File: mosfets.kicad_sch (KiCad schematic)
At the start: 25 parts, among them IC2 IRFR9014PBF, J4 Screw_Terminal_01x02, J5 Screw_Terminal_01x02, J6 Screw_Terminal_01x02, J7 Screw_Terminal_01x02, J8 Screw_Terminal_01x02, J9 Screw_Terminal_01x02, Q1 DMN3404L, Q2 DMN3404L, Q3 DMN3404L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

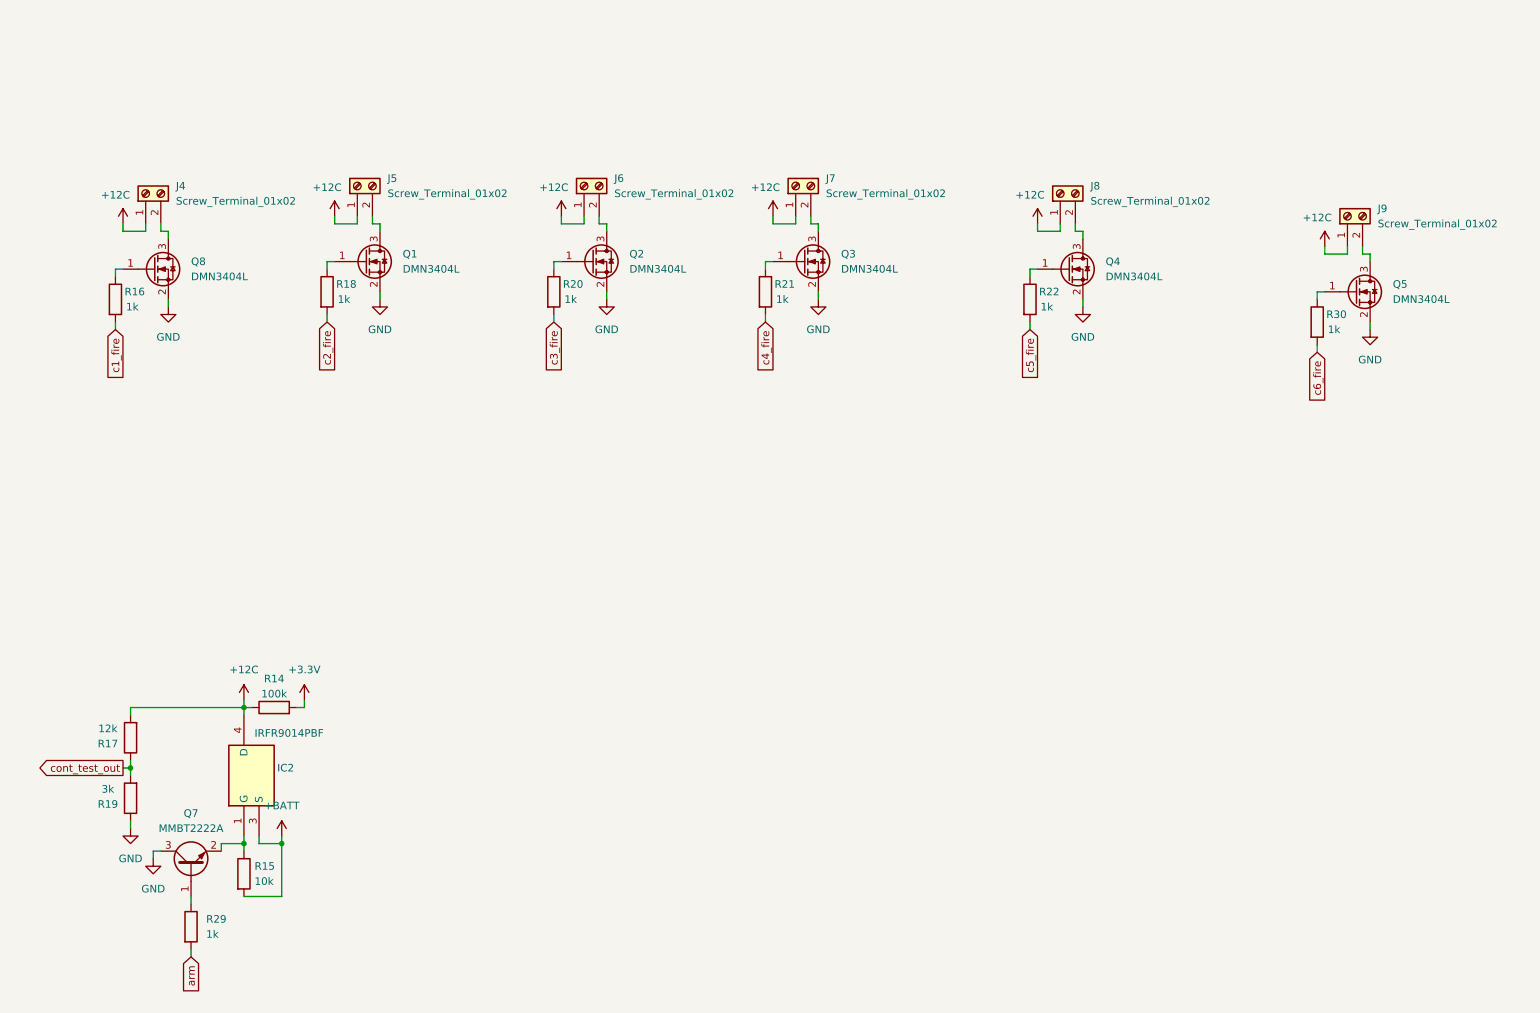
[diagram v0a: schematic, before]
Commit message: placed mosfet stuff, probably all that's left is add pull resistors on the nfets and finish routing the fets
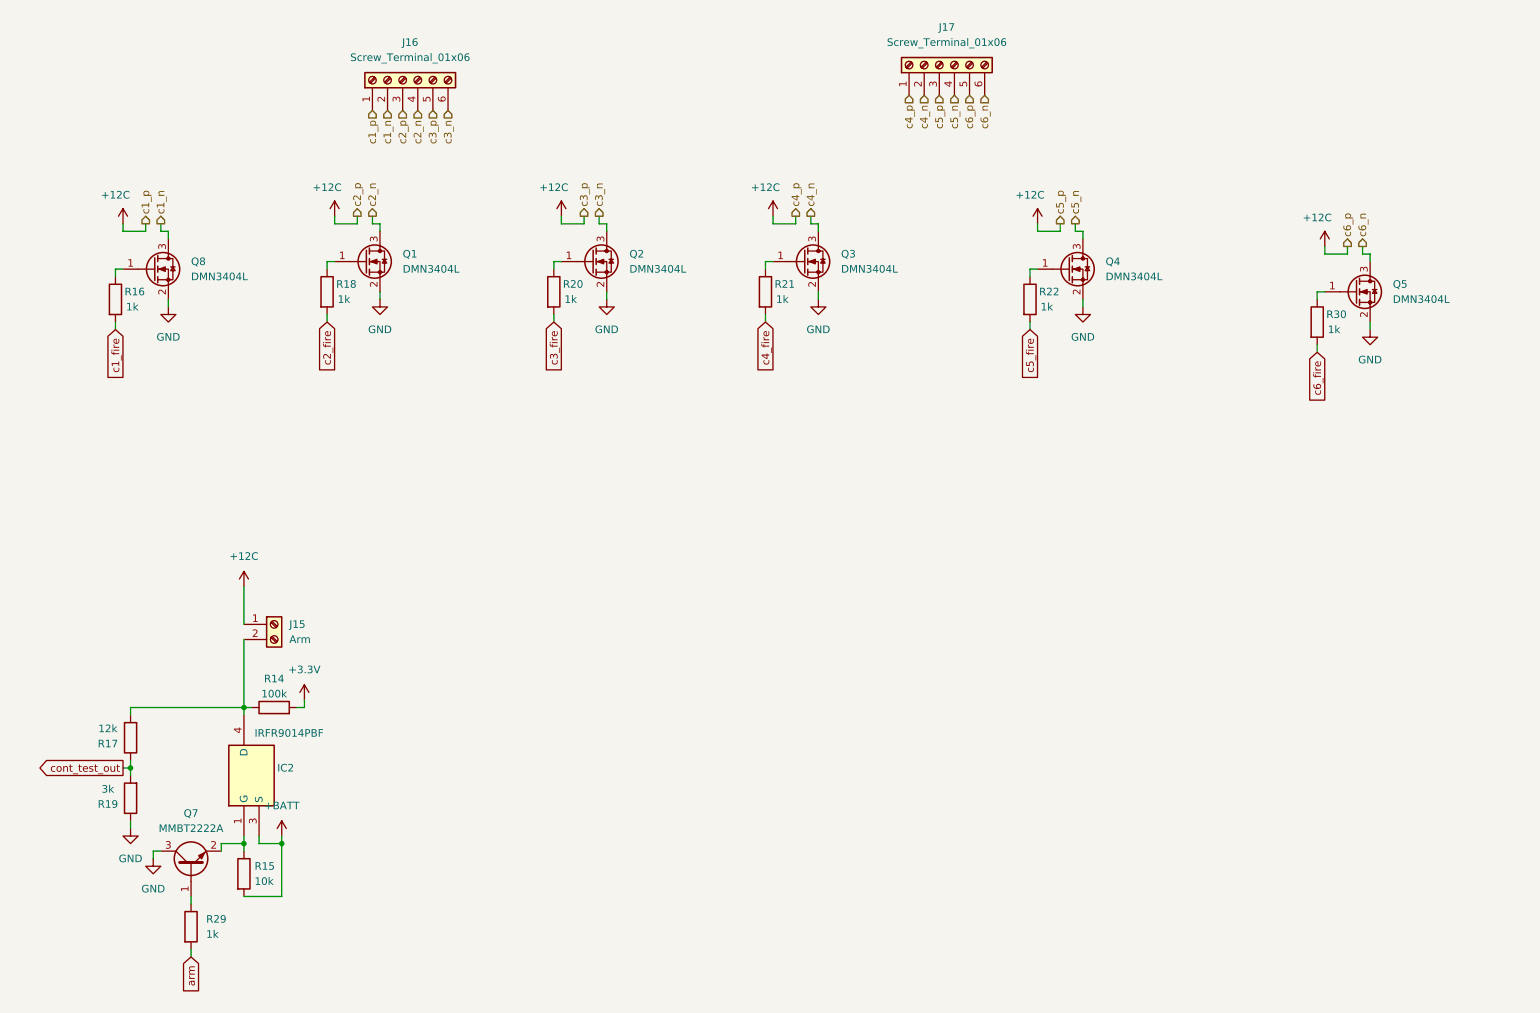
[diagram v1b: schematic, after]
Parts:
- removed J4, J5, J6, J7, J8, J9: Screw_Terminal_01x02, TerminalBlock:TerminalBlock_Xinya_XY308-2.54-2P_1x02_P2.54mm_Horizontal, symbol Connector:Screw_Terminal_01x02
- added J15: Arm, TerminalBlock:TerminalBlock_Xinya_XY308-2.54-2P_1x02_P2.54mm_Horizontal, symbol Connector:Screw_Terminal_01x02
- added J16, J17: Screw_Terminal_01x06, TerminalBlock:TerminalBlock_Xinya_XY308-2.54-6P_1x06_P2.54mm_Horizontal, symbol Connector:Screw_Terminal_01x06
- R14, R15, R16, R17, R18, R19, R20, R21, R22, R30: footprint Resistor_SMD:R_0603_1608Metric -> Resistor_SMD:R_0402_1005Metric
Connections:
- net +12C: now also J15.1 (Pin_1), J16.1 (Pin_1), J16.3 (Pin_3), J16.5 (Pin_5), J17.1 (Pin_1), J17.3 (Pin_3), J17.5 (Pin_5); no longer IC2.4 (D), R14.1, R17.2
- net c4_n: now reaches Q3.3 (D)
- net c4_n: now also J17.2 (Pin_2)
- net c1_n: now reaches Q8.3 (D)
- net c1_n: now also J16.2 (Pin_2)
- net c5_n: now reaches Q4.3 (D)
- net c5_n: now also J17.4 (Pin_4)
- net c2_n: now reaches Q1.3 (D)
- net c2_n: now also J16.4 (Pin_4)
- net c6_n: now reaches Q5.3 (D)
- net c6_n: now also J17.6 (Pin_6)
- net c3_n: now reaches Q2.3 (D)
- net c3_n: now also J16.6 (Pin_6)
- new net: IC2.4 (D), J15.2 (Pin_2), R14.1, R17.2

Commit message: idk what I did but it wasn't saved
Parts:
- removed J16, J17: Screw_Terminal_01x06, TerminalBlock:TerminalBlock_Xinya_XY308-2.54-6P_1x06_P2.54mm_Horizontal, symbol Connector:Screw_Terminal_01x06
- added J4: Screw_Terminal_01x12, TerminalBlock:TerminalBlock_Xinya_XY308-2.54-12P_1x12_P2.54mm_Horizontal, symbol Connector:Screw_Terminal_01x12
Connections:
- net +12C: now also J4.10 (Pin_10), J4.12 (Pin_12), J4.2 (Pin_2), J4.4 (Pin_4), J4.6 (Pin_6), J4.8 (Pin_8)
- net c1_n: now also J4.11 (Pin_11)
- net c2_n: now also J4.9 (Pin_9)
- net c3_n: now also J4.7 (Pin_7)
- net c4_n: now also J4.5 (Pin_5)
- net c5_n: now also J4.3 (Pin_3)
- net c6_n: now also J4.1 (Pin_1)
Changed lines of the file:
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@@
 	(hierarchical_label "c1_n"
 		(shape input)
-		(at 83.82 38.1 270)
+		(at 137.16 34.29 270)
 		(effects
 			(font
@@
 	(hierarchical_label "c3_p"
 		(shape input)
-		(at 91.44 38.1 270)
+		(at 129.54 34.29 270)
 		(effects
 			(font
@@
 	(hierarchical_label "c5_p"
 		(shape input)
-		(at 176.53 35.56 270)
+		(at 119.38 34.29 270)
 		(effects
 			(font
@@
 	(hierarchical_label "c2_p"
 		(shape input)
-		(at 86.36 38.1 270)
+		(at 134.62 34.29 270)
 		(effects
 			(font
@@
 	(hierarchical_label "c3_n"
 		(shape input)
-		(at 93.98 38.1 270)
+		(at 127 34.29 270)
 		(effects
 			(font
@@
 	(hierarchical_label "c6_n"
 		(shape input)
-		(at 184.15 35.56 270)
+		(at 111.76 34.29 270)
 		(effects
 			(font
@@
 	(hierarchical_label "c4_p"
 		(shape input)
-		(at 171.45 35.56 270)
+		(at 124.46 34.29 270)
 		(effects
 			(font
@@
 	(hierarchical_label "c5_n"
 		(shape input)
-		(at 179.07 35.56 270)
+		(at 116.84 34.29 270)
 		(effects
 			(font
@@
 	(hierarchical_label "c4_n"
 		(shape input)
-		(at 173.99 35.56 270)
+		(at 121.92 34.29 270)
 		(effects
 			(font
@@
 	(hierarchical_label "c1_p"
 		(shape input)
-		(at 81.28 38.1 270)
+		(at 139.7 34.29 270)
 		(effects
 			(font
@@
 	(hierarchical_label "c6_p"
 		(shape input)
-		(at 181.61 35.56 270)
+		(at 114.3 34.29 270)
 		(effects
 			(font
@@
 	(hierarchical_label "c2_n"
 		(shape input)
-		(at 88.9 38.1 270)
+		(at 132.08 34.29 270)
 		(effects
 			(font
@@
 	)
 	(symbol
+		(lib_id "Connector:Screw_Terminal_01x12")
+		(at 124.46 29.21 90)
+		(unit 1)
+		(exclude_from_sim no)
+		(in_bom yes)
+		(on_board yes)
+		(dnp no)
+		(fields_autoplaced yes)
+		(property "Reference" "J4"
+			(at 125.73 22.86 90)
+			(effects
+				(font
+					(size 1.27 1.27)
+				)
+			)
+		)
+		(property "Value" "Screw_Terminal_01x12"
+			(at 125.73 25.4 90)
+			(effects
+				(font
+					(size 1.27 1.27)
+				)
+			)
+		)
+		(property "Footprint" "TerminalBlock:TerminalBlock_Xinya_XY308-2.54-12P_1x12_P2.54mm_Horizontal"
+			(at 124.46 29.21 0)
+			(effects
+				(font
+					(size 1.27 1.27)
+				)
+				(hide yes)
+			)
+		)
+		(property "Datasheet" "~"
+			(at 124.46 29.21 0)
+			(effects
+				(font
+					(size 1.27 1.27)
+				)
+				(hide yes)
+			)
+		)
+		(property "Description" "Generic screw terminal, single row, 01x12, script generated (kicad-library-utils/schlib/autogen/connector/)"
+			(at 124.46 29.21 0)
+			(effects
+				(font
+					(size 1.27 1.27)
+				)
+				(hide yes)
+			)
+		)
+		(pin "6"
+		)
+		(pin "10"
+		)
+		(pin "1"
+		)
+		(pin "7"
+		)
+		(pin "5"
+		)
+		(pin "4"
+		)
+		(pin "3"
+		)
+		(pin "12"
+		)
+		(pin "11"
+		)
+		(pin "2"
+		)
+		(pin "9"
+		)
+		(pin "8"
+		)
+		(instances
+			(project ""
+				(path "/d0cafa98-cc2a-4ab3-8dbc-f937bedf434b/95cda17b-9612-4f29-a3fa-5878468b6ce9"
+					(reference "J4")
+					(unit 1)
+				)
+			)
+		)
+	)
+	(symbol
 		(lib_id "power:+12C")
 		(at 74.93 55.88 0)
@@
 	)
 	(symbol
-		(lib_id "Connector:Screw_Terminal_01x06")
-		(at 86.36 33.02 90)
-		(unit 1)
-		(exclude_from_sim no)
-		(in_bom yes)
-		(on_board yes)
-		(dnp no)
-		(fields_autoplaced yes)
-		(property "Reference" "J16"
-			(at 87.63 26.67 90)
-			(effects
-				(font
-					(size 1.27 1.27)
-				)
-			)
-		)
-		(property "Value" "Screw_Terminal_01x06"
-			(at 87.63 29.21 90)
-			(effects
-				(font
-					(size 1.27 1.27)
-				)
-			)
-		)
-		(property "Footprint" "TerminalBlock:TerminalBlock_Xinya_XY308-2.54-6P_1x06_P2.54mm_Horizontal"
-			(at 86.36 33.02 0)
-			(effects
-				(font
-					(size 1.27 1.27)
-				)
-				(hide yes)
-			)
-		)
-		(property "Datasheet" "~"
-			(at 86.36 33.02 0)
-			(effects
-				(font
-					(size 1.27 1.27)
-				)
-				(hide yes)
-			)
-		)
-		(property "Description" "Generic screw terminal, single row, 01x06, script generated (kicad-library-utils/schlib/autogen/connector/)"
-			(at 86.36 33.02 0)
-			(effects
-				(font
-					(size 1.27 1.27)
-				)
-				(hide yes)
-			)
-		)
-		(pin "4"
-		)
-		(pin "3"
-		)
-		(pin "2"
-		)
-		(pin "5"
-		)
-		(pin "1"
-		)
-		(pin "6"
-		)
-		(instances
-			(project ""
-				(path "/d0cafa98-cc2a-4ab3-8dbc-f937bedf434b/95cda17b-9612-4f29-a3fa-5878468b6ce9"
-					(reference "J16")
-					(unit 1)
-				)
-			)
-		)
-	)
-	(symbol
 		(lib_id "Device:R")
 		(at 38.1 69.85 0)
@@
 					(unit 1)
 				)
-			)
-		)
-	)
-	(symbol
-		(lib_id "Connector:Screw_Terminal_01x06")
-		(at 176.53 30.48 90)
-		(unit 1)
-		(exclude_from_sim no)
-		(in_bom yes)
-		(on_board yes)
-		(dnp no)
-		(fields_autoplaced yes)
-		(property "Reference" "J17"
-			(at 177.8 24.13 90)
-			(effects
-				(font
-					(size 1.27 1.27)
-				)
-			)
-		)
-		(property "Value" "Screw_Terminal_01x06"
-			(at 177.8 26.67 90)
-			(effects
-				(font
-					(size 1.27 1.27)
-				)
-			)
-		)
-		(property "Footprint" "TerminalBlock:TerminalBlock_Xinya_XY308-2.54-6P_1x06_P2.54mm_Horizontal"
-			(at 176.53 30.48 0)
-			(effects
-				(font
-					(size 1.27 1.27)
-				)
-				(hide yes)
-			)
-		)
-		(property "Datasheet" "~"
-			(at 176.53 30.48 0)
-			(effects
-				(font
-					(size 1.27 1.27)
-				)
-				(hide yes)
-			)
-		)
-		(property "Description" "Generic screw terminal, single row, 01x06, script generated (kicad-library-utils/schlib/autogen/connector/)"
-			(at 176.53 30.48 0)
-			(effects
-				(font
-					(size 1.27 1.27)
-				)
-				(hide yes)
-			)
-		)
-		(pin "4"
-		)
-		(pin "3"
-		)
-		(pin "2"
-		)
-		(pin "5"
-		)
-		(pin "1"
-		)
-		(pin "6"
-		)
-		(instances
-			(project "stDevboard"
-				(path "/d0cafa98-cc2a-4ab3-8dbc-f937bedf434b/95cda17b-9612-4f29-a3fa-5878468b6ce9"
-					(reference "J17")
-					(unit 1)
-				)
